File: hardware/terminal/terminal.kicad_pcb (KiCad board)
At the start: 2 copper layers, 60 x 40 mm, 30 parts, among them IC1 ATMEGA8-P, J1 RJ45, P1 Prog, P10 CONN_4, P11 CONN_5X2, P12 CONN_4, P13 CONN_3X2, P14 CONN_5X2, P2 RC522, P3 LCD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

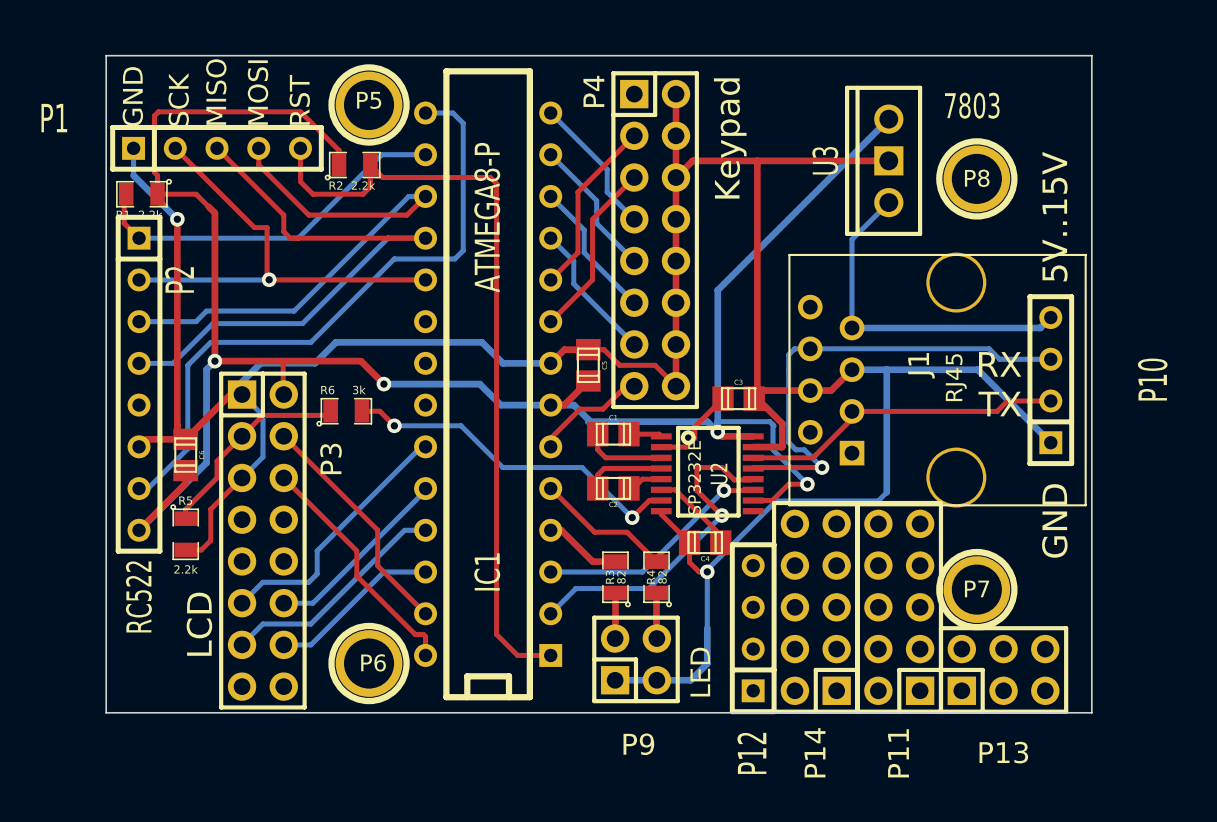
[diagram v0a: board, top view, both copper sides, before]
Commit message: o Add background light option. o Better labeling on both sides of the board.
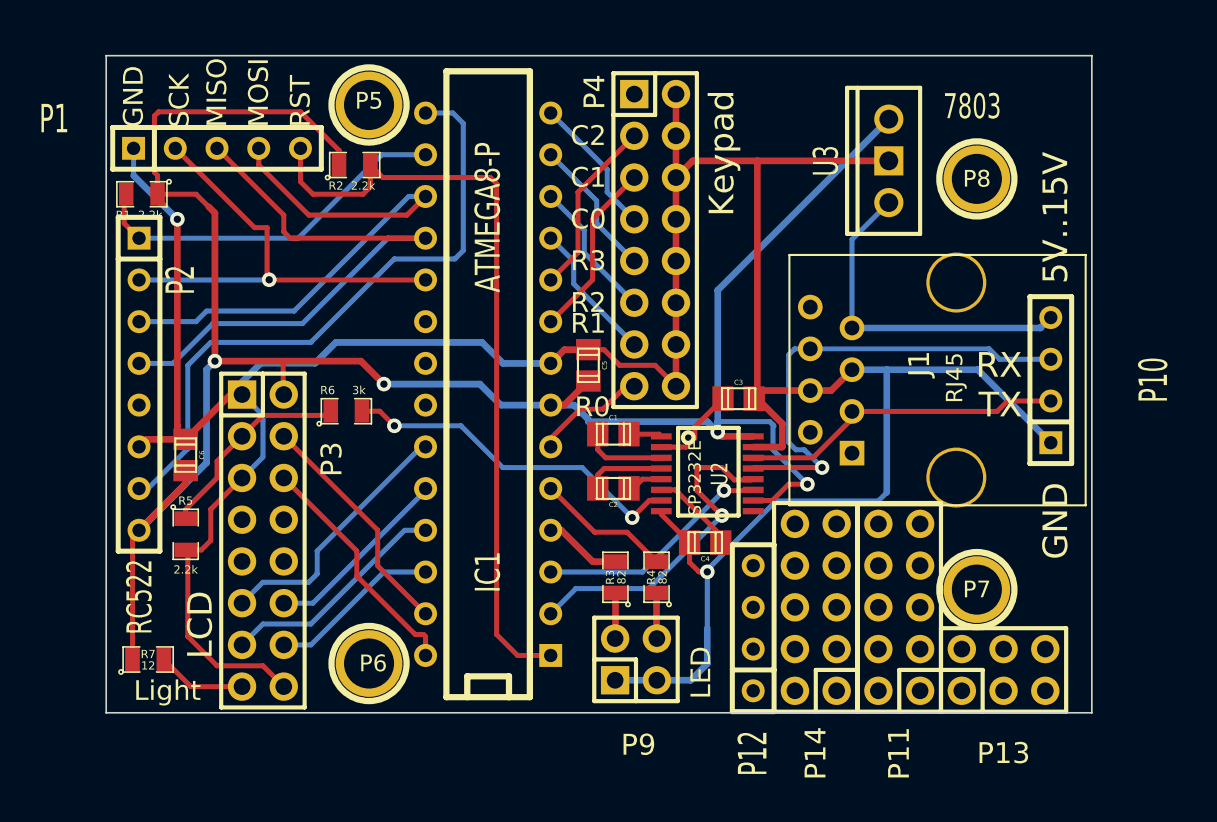
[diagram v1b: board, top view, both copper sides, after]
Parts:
- added R7: 12, SMD_Packages:SMD-0805, F.Cu at (122.6, 71.8)
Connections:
- P3 pad 16: Net-(P3-Pad16) -> GND
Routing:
- net GND: track 178.9 -> 191.4 mm
- net +3.3V: track 123.0 -> 131.0 mm
- net Net-(P3-Pad15): track 0.00 -> 5.45 mm
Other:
- board text added: "C0"
- board text added: "C1"
- board text added: "C2"
- board text added: "Light"
- board text added: "R0"
- board text added: "R1"
- board text added: "R2"
- board text added: "R3"

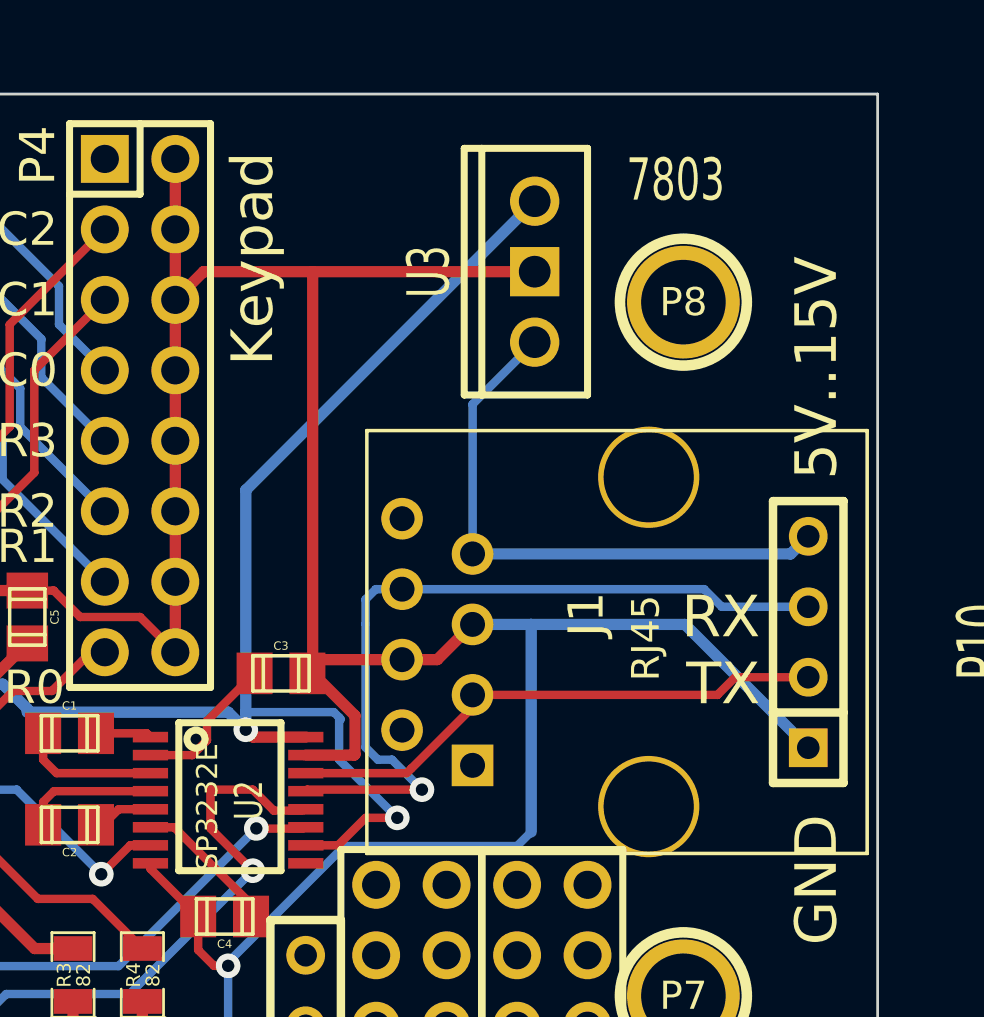
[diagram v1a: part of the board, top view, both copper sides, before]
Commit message: o Wider tracks for power.
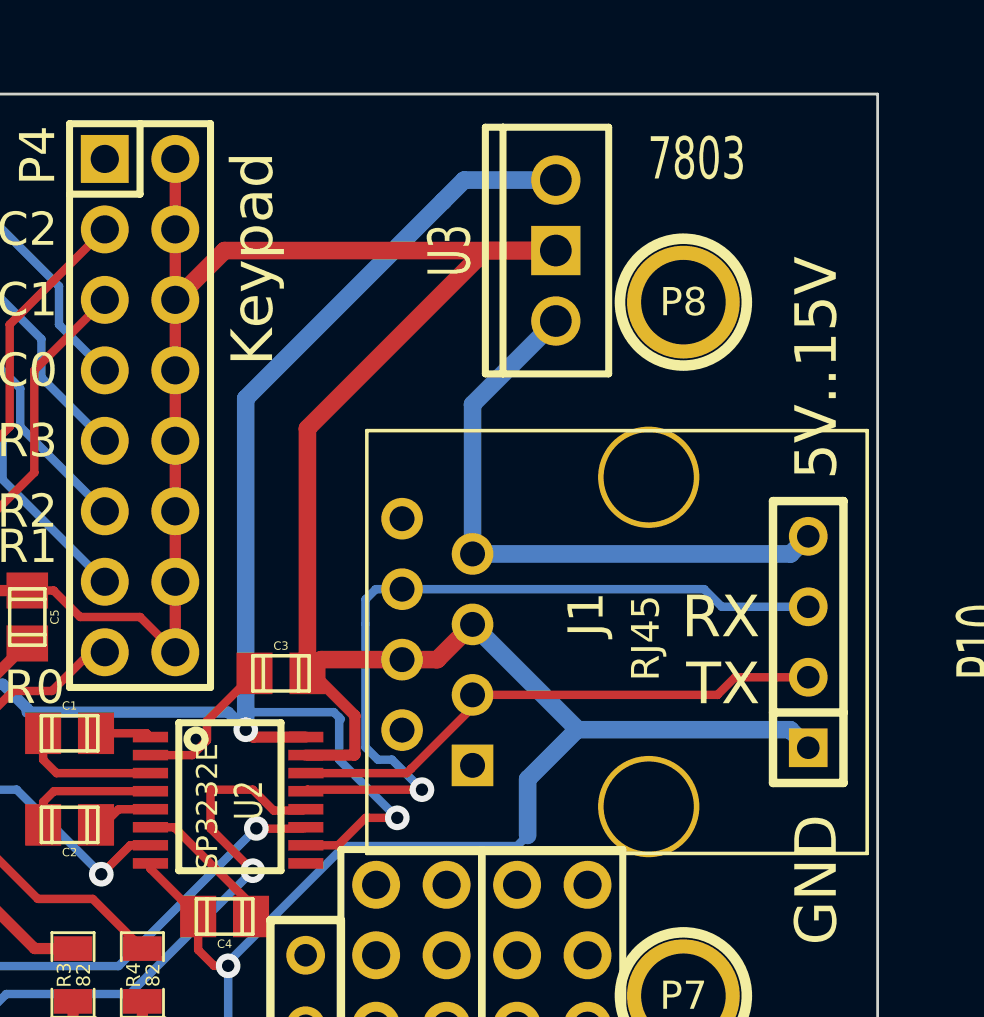
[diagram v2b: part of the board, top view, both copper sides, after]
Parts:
- moved U3 1.08 mm to (168.4, 40.6)
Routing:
- net +3.3V: track 131.0 -> 142.6 mm
- net GND: track 191.4 -> 196.4 mm
- net +12V: track 20.9 -> 22.0 mm
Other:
- net class Default: trace_width 0.3048 -> 0.635
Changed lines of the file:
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@@
     (thickness 1.6)
     (drawings 43)
-    (tracks 323)
+    (tracks 330)
     (zones 0)
     (modules 31)
@@
   )
   (setup
-    (last_trace_width 0.3048)
+    (last_trace_width 0.635)
     (trace_clearance 0.2032)
     (zone_clearance 0.508)
@@
   (net_class Default "This is the default net class."
     (clearance 0.2032)
-    (trace_width 0.3048)
+    (trace_width 0.635)
     (via_dia 0.889)
     (via_drill 0.635)
@@
   )
   (module Discret:LM78XXV (layer F.Cu)
-    (at 167.64 41.402 180)
+    (at 168.402 40.64 180)
     (descr "Regulateur TO220 serie LM78xx")
     (tags "TR TO220")
@@
   (segment (start 152.64638 60.77712) (end 153.79192 60.77712) (width 0.3048) (layer F.Cu) (net 4))
   (segment (start 151.8285 61.595) (end 152.64638 60.77712) (width 0.3048) (layer F.Cu) (net 4))
-  (segment (start 124.841 65.0875) (end 124.968 65.2145) (width 0.3048) (layer F.Cu) (net 5) (status C00000))
-  (segment (start 124.968 65.2145) (end 124.968 70.358) (width 0.3048) (layer F.Cu) (net 5) (status 400000))
-  (segment (start 129.54 72.136) (end 130.81 73.406) (width 0.3048) (layer F.Cu) (net 5) (status 800000))
+  (segment (start 169.1805 57.8955) (end 167.386 59.69) (width 0.635) (layer B.Cu) (net 5))
+  (segment (start 167.386 59.69) (end 167.386 61.722) (width 0.635) (layer B.Cu) (net 5))
+  (segment (start 165.4 54.115) (end 169.1805 57.8955) (width 0.635) (layer B.Cu) (net 5) (status 400000))
+  (segment (start 169.1805 57.8955) (end 169.197 57.912) (width 0.635) (layer B.Cu) (net 5))
+  (segment (start 169.197 57.912) (end 176.852 57.912) (width 0.635) (layer B.Cu) (net 5) (status 800000))
+  (segment (start 176.852 57.912) (end 177.5 58.56) (width 0.635) (layer B.Cu) (net 5) (status C00000))
+  (segment (start 165.4 54.115) (end 164.13 55.385) (width 0.635) (layer F.Cu) (net 5) (status 400000))
+  (segment (start 164.13 55.385) (end 159.9435 55.385) (width 0.635) (layer F.Cu) (net 5) (status 800000))
+  (segment (start 159.9435 55.385) (end 159.4485 55.88) (width 0.635) (layer F.Cu) (net 5) (status C00000))
+  (segment (start 168.402 40.64) (end 165.862 40.64) (width 0.635) (layer F.Cu) (net 5) (status 400000))
+  (segment (start 159.4485 47.0535) (end 159.4485 55.88) (width 0.635) (layer F.Cu) (net 5) (status 800000))
+  (segment (start 165.862 40.64) (end 159.4485 47.0535) (width 0.635) (layer F.Cu) (net 5))
+  (segment (start 154.686 42.418) (end 156.464 40.64) (width 0.635) (layer F.Cu) (net 5) (status 400000))
+  (segment (start 156.464 40.64) (end 168.402 40.64) (width 0.635) (layer F.Cu) (net 5) (status 800000))
+  (segment (start 124.841 65.0875) (end 124.968 65.2145) (width 0.3048) (layer F.Cu) (net 5))
+  (segment (start 124.968 65.2145) (end 124.968 70.358) (width 0.3048) (layer F.Cu) (net 5))
+  (segment (start 129.54 72.136) (end 130.81 73.406) (width 0.3048) (layer F.Cu) (net 5))
   (segment (start 126.746 72.136) (end 129.54 72.136) (width 0.3048) (layer F.Cu) (net 5))
   (segment (start 124.968 70.358) (end 126.746 72.136) (width 0.3048) (layer F.Cu) (net 5))
@@
   (segment (start 154.686 39.878) (end 154.686 42.418) (width 0.4064) (layer F.Cu) (net 5))
   (segment (start 154.686 37.338) (end 154.686 39.878) (width 0.4064) (layer F.Cu) (net 5))
-  (segment (start 159.639 41.402) (end 155.702 41.402) (width 0.4064) (layer F.Cu) (net 5))
-  (segment (start 167.64 41.402) (end 159.639 41.402) (width 0.4064) (layer F.Cu) (net 5))
-  (segment (start 155.702 41.402) (end 154.686 42.418) (width 0.4064) (layer F.Cu) (net 5))
   (segment (start 128.23 54.904) (end 128.23 55.61) (width 0.4064) (layer B.Cu) (net 5))
   (segment (start 144.154 53.73) (end 142.875 52.451) (width 0.4064) (layer B.Cu) (net 5))
@@
   (segment (start 128.23 55.61) (end 127.5875 55.61) (width 0.4064) (layer F.Cu) (net 5))
   (segment (start 124.841 58.3565) (end 124.333 57.8485) (width 0.4064) (layer F.Cu) (net 5))
-  (segment (start 167.513 54.115) (end 165.4 54.115) (width 0.4064) (layer B.Cu) (net 5))
-  (segment (start 173.055 54.115) (end 167.513 54.115) (width 0.4064) (layer B.Cu) (net 5))
-  (segment (start 177.5 58.56) (end 173.055 54.115) (width 0.4064) (layer B.Cu) (net 5))
   (segment (start 147.8945 52.8955) (end 147.06 53.73) (width 0.4064) (layer F.Cu) (net 5))
   (segment (start 149.352 52.8955) (end 147.8945 52.8955) (width 0.4064) (layer F.Cu) (net 5))
@@
   (segment (start 161.163 57.404) (end 161.163 58.801) (width 0.4064) (layer F.Cu) (net 5))
   (segment (start 159.39008 58.8264) (end 161.1376 58.8264) (width 0.4064) (layer F.Cu) (net 5))
-  (segment (start 159.9435 55.385) (end 162.86 55.385) (width 0.4064) (layer F.Cu) (net 5))
   (segment (start 159.4485 55.88) (end 159.9435 55.385) (width 0.4064) (layer F.Cu) (net 5))
-  (segment (start 159.639 55.6895) (end 159.639 41.402) (width 0.4064) (layer F.Cu) (net 5))
   (segment (start 159.4485 55.88) (end 159.639 55.6895) (width 0.4064) (layer F.Cu) (net 5))
-  (segment (start 164.13 55.385) (end 162.86 55.385) (width 0.4064) (layer F.Cu) (net 5))
-  (segment (start 165.4 54.115) (end 164.13 55.385) (width 0.4064) (layer F.Cu) (net 5))
   (segment (start 153.52 73.02) (end 150.98 73.02) (width 0.4064) (layer B.Cu) (net 5))
   (segment (start 126.365 62.611) (end 126.365 64.516) (width 0.3048) (layer F.Cu) (net 5))
@@
   (segment (start 156.591 66.294) (end 156.591 69.85) (width 0.3048) (layer B.Cu) (net 5))
   (segment (start 156.591 72.009) (end 155.58 73.02) (width 0.4064) (layer B.Cu) (net 5))
-  (segment (start 167.513 61.595) (end 167.513 54.115) (width 0.4064) (layer B.Cu) (net 5))
   (segment (start 160.782 62.103) (end 156.591 66.294) (width 0.3048) (layer B.Cu) (net 5))
+  (segment (start 167.386 61.722) (end 167.005 62.103) (width 0.3048) (layer B.Cu) (net 5))
   (segment (start 167.005 62.103) (end 160.782 62.103) (width 0.3048) (layer B.Cu) (net 5))
-  (segment (start 167.513 61.595) (end 167.005 62.103) (width 0.3048) (layer B.Cu) (net 5))
+  (segment (start 167.513 61.595) (end 167.386 61.722) (width 0.3048) (layer B.Cu) (net 5))
   (via (at 156.591 66.421) (size 0.889) (layers F.Cu B.Cu) (net 5))
   (segment (start 156.591 66.421) (end 156.591 66.294) (width 0.3048) (layer B.Cu) (net 5))
@@
   (segment (start 151.638 55.118) (end 150.241 56.515) (width 0.3048) (layer F.Cu) (net 12))
   (segment (start 152.146 55.118) (end 151.638 55.118) (width 0.3048) (layer F.Cu) (net 12))
-  (segment (start 122 63.89) (end 121.6025 64.2875) (width 0.3048) (layer F.Cu) (net 13) (status C00000))
-  (segment (start 121.6025 64.2875) (end 121.6025 71.755) (width 0.3048) (layer F.Cu) (net 13) (status C00000))
+  (segment (start 168.402 38.1) (end 165.1 38.1) (width 0.635) (layer B.Cu) (net 13) (status 400000))
+  (segment (start 164.338 38.862) (end 157.226 45.974) (width 0.635) (layer B.Cu) (net 13))
+  (segment (start 157.226 45.974) (end 157.226 57.912) (width 0.635) (layer B.Cu) (net 13))
+  (segment (start 165.1 38.1) (end 164.338 38.862) (width 0.635) (layer B.Cu) (net 13))
+  (segment (start 122 63.89) (end 121.6025 64.2875) (width 0.3048) (layer F.Cu) (net 13))
+  (segment (start 121.6025 64.2875) (end 121.6025 71.755) (width 0.3048) (layer F.Cu) (net 13))
   (segment (start 123.1265 43.434) (end 123.1265 42.291) (width 0.3048) (layer F.Cu) (net 13))
   (segment (start 134.1755 40.767) (end 134.1755 41.656) (width 0.3048) (layer F.Cu) (net 13))
@@
   (segment (start 157.226 57.912) (end 157.49016 58.17616) (width 0.4064) (layer F.Cu) (net 13))
   (segment (start 157.49016 58.17616) (end 159.39008 58.17616) (width 0.4064) (layer F.Cu) (net 13))
-  (segment (start 167.64 38.862) (end 157.226 49.276) (width 0.4064) (layer B.Cu) (net 13))
   (segment (start 157.226 57.277) (end 157.226 57.912) (width 0.4064) (layer B.Cu) (net 13))
   (segment (start 157.226 49.276) (end 157.226 57.277) (width 0.4064) (layer B.Cu) (net 13))
@@
   (segment (start 139.44 70.352) (end 139.44 71.51) (width 0.3048) (layer F.Cu) (net 32))
   (segment (start 130.81 60.706) (end 135.255 65.151) (width 0.3048) (layer F.Cu) (net 32))
-  (segment (start 176.865 51.575) (end 165.4 51.575) (width 0.4064) (layer B.Cu) (net 35))
-  (segment (start 177.5 50.94) (end 176.865 51.575) (width 0.4064) (layer B.Cu) (net 35))
-  (segment (start 165.4 46.182) (end 165.4 51.575) (width 0.3048) (layer B.Cu) (net 35))
-  (segment (start 167.64 43.942) (end 165.4 46.182) (width 0.3048) (layer B.Cu) (net 35))
-  (segment (start 123.5075 71.755) (end 125.1585 73.406) (width 0.3048) (layer F.Cu) (net 41) (status 400000))
-  (segment (start 125.1585 73.406) (end 128.27 73.406) (width 0.3048) (layer F.Cu) (net 41) (status 800000))
+  (segment (start 177.5 50.94) (end 176.865 51.575) (width 0.635) (layer B.Cu) (net 35) (status 400000))
+  (segment (start 176.865 51.575) (end 165.4 51.575) (width 0.635) (layer B.Cu) (net 35) (status 800000))
+  (segment (start 168.402 43.18) (end 165.4 46.182) (width 0.635) (layer B.Cu) (net 35) (status 400000))
+  (segment (start 165.4 46.182) (end 165.4 51.575) (width 0.635) (layer B.Cu) (net 35))
+  (segment (start 123.5075 71.755) (end 125.1585 73.406) (width 0.3048) (layer F.Cu) (net 41))
+  (segment (start 125.1585 73.406) (end 128.27 73.406) (width 0.3048) (layer F.Cu) (net 41))
   (segment (start 165.4 57.104) (end 165.4 56.655) (width 0.3048) (layer F.Cu) (net 48))
   (segment (start 174.231 56.655) (end 174.866 56.02) (width 0.3048) (layer F.Cu) (net 48))
